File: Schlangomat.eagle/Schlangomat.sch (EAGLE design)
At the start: 38 parts, among them IC1 ULN2003AN, J1 Sensor1, J2 Sensor2, K1 36.11, K2 36.11, K3 36.11, K4 36.11, Q1 16MHz

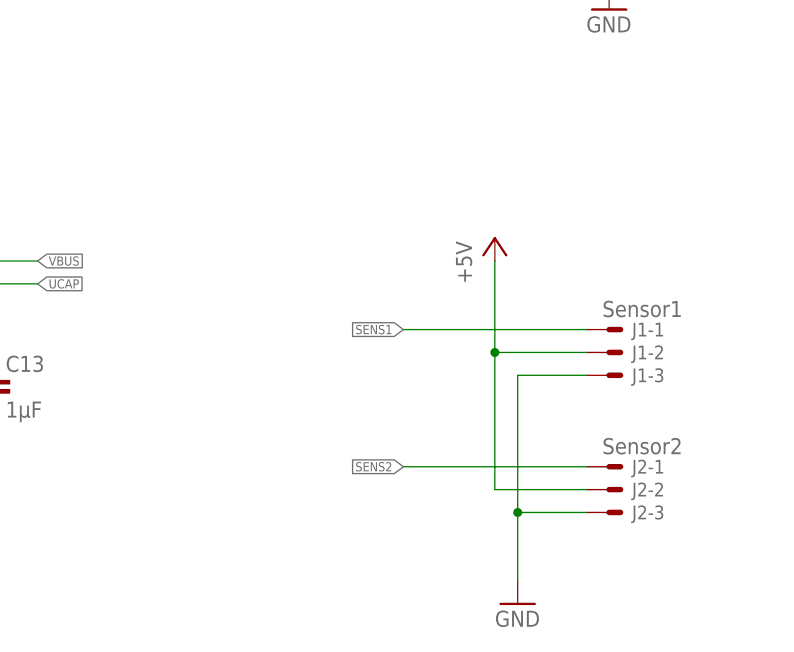
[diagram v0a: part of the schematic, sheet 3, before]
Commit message: Sensor-Support eingebaut
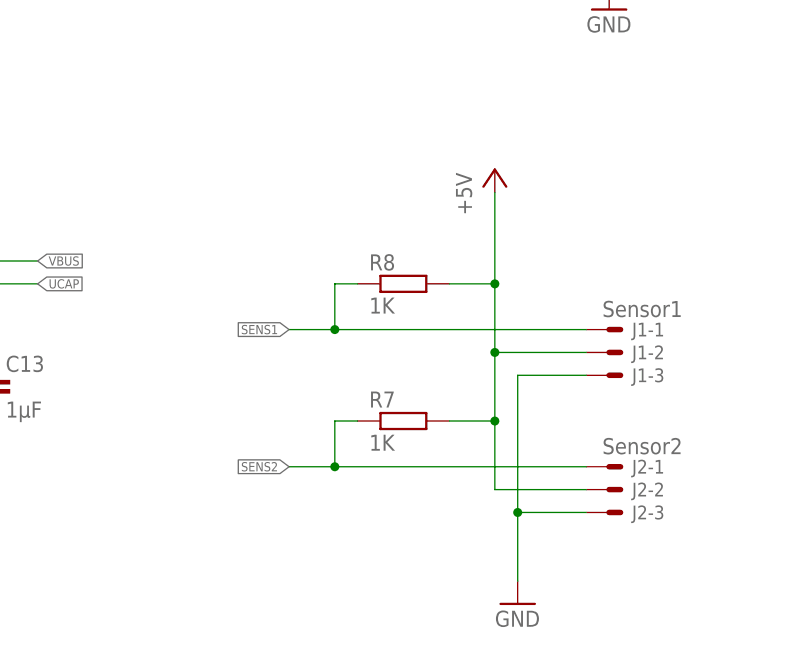
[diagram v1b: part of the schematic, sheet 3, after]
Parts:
- added R7, R8: 1K, rcl:R-EU_M0805
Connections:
- net +5V: now also R7.2, R8.2
- net SENS1: now also R8.1
- net SENS2: now also R7.1
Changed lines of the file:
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@@
 <part name="P+7" library="supply1" deviceset="+5V" device=""/>
 <part name="GND9" library="supply1" deviceset="GND" device=""/>
+<part name="R7" library="rcl" deviceset="R-EU_" device="M0805" value="1K"/>
+<part name="R8" library="rcl" deviceset="R-EU_" device="M0805" value="1K"/>
 </parts>
 <sheets>
@@
 <instance part="J2" gate="-2" x="185.42" y="0"/>
 <instance part="J2" gate="-3" x="185.42" y="-2.54"/>
-<instance part="P+7" gate="1" x="172.72" y="27.94"/>
+<instance part="P+7" gate="1" x="172.72" y="35.56"/>
 <instance part="GND9" gate="1" x="175.26" y="-12.7"/>
+<instance part="R7" gate="G$1" x="162.56" y="7.62"/>
+<instance part="R8" gate="G$1" x="162.56" y="22.86"/>
 </instances>
 <busses>
@@
 <pinref part="J2" gate="-2" pin="S"/>
 <wire x1="182.88" y1="0" x2="172.72" y2="0" width="0.1524" layer="91"/>
-<wire x1="172.72" y1="0" x2="172.72" y2="15.24" width="0.1524" layer="91"/>
+<wire x1="172.72" y1="0" x2="172.72" y2="7.62" width="0.1524" layer="91"/>
 <junction x="172.72" y="15.24"/>
 <pinref part="P+7" gate="1" pin="+5V"/>
-<wire x1="172.72" y1="25.4" x2="172.72" y2="15.24" width="0.1524" layer="91"/>
+<wire x1="172.72" y1="7.62" x2="172.72" y2="15.24" width="0.1524" layer="91"/>
+<wire x1="172.72" y1="33.02" x2="172.72" y2="22.86" width="0.1524" layer="91"/>
+<pinref part="R8" gate="G$1" pin="2"/>
+<wire x1="172.72" y1="22.86" x2="172.72" y2="15.24" width="0.1524" layer="91"/>
+<wire x1="172.72" y1="22.86" x2="167.64" y2="22.86" width="0.1524" layer="91"/>
+<junction x="172.72" y="22.86"/>
+<pinref part="R7" gate="G$1" pin="2"/>
+<wire x1="167.64" y1="7.62" x2="172.72" y2="7.62" width="0.1524" layer="91"/>
+<junction x="172.72" y="7.62"/>
 </segment>
 </net>
@@
 <segment>
 <pinref part="J1" gate="-1" pin="S"/>
-<wire x1="182.88" y1="17.78" x2="162.56" y2="17.78" width="0.1524" layer="91"/>
-<label x="162.56" y="17.78" size="1.016" layer="95" rot="R180" xref="yes"/>
+<wire x1="182.88" y1="17.78" x2="154.94" y2="17.78" width="0.1524" layer="91"/>
+<label x="149.86" y="17.78" size="1.016" layer="95" rot="R180" xref="yes"/>
+<pinref part="R8" gate="G$1" pin="1"/>
+<wire x1="154.94" y1="17.78" x2="149.86" y2="17.78" width="0.1524" layer="91"/>
+<wire x1="157.48" y1="22.86" x2="154.94" y2="22.86" width="0.1524" layer="91"/>
+<wire x1="154.94" y1="22.86" x2="154.94" y2="17.78" width="0.1524" layer="91"/>
+<junction x="154.94" y="17.78"/>
 </segment>
 </net>
@@
 <segment>
 <pinref part="J2" gate="-1" pin="S"/>
-<wire x1="182.88" y1="2.54" x2="162.56" y2="2.54" width="0.1524" layer="91"/>
-<label x="162.56" y="2.54" size="1.016" layer="95" rot="R180" xref="yes"/>
-</segment>
-</net>
+<wire x1="182.88" y1="2.54" x2="154.94" y2="2.54" width="0.1524" layer="91"/>
+<label x="149.86" y="2.54" size="1.016" layer="95" rot="R180" xref="yes"/>
+<pinref part="R7" gate="G$1" pin="1"/>
+<wire x1="154.94" y1="2.54" x2="149.86" y2="2.54" width="0.1524" layer="91"/>
+<wire x1="157.48" y1="7.62" x2="154.94" y2="7.62" width="0.1524" layer="91"/>
+<wire x1="154.94" y1="7.62" x2="154.94" y2="2.54" width="0.1524" layer="91"/>
+<junction x="154.94" y="2.54"/>
+</segment>
+</net>

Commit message: Board gelayoutet
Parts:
- removed IN: (no value), con-ptr500:AK500/2
- removed OUT: (no value), con-ptr500:AK500/4
- removed SENS1, SENS2: 22-27-2031-03, con-molex:22-27-2031-03
- added X1: AC-IN, con-wago:236-501-7,62
- added X2: AC-OUT-1, con-wago:236-501-7,62
- added X3: AC-OUT-2, con-wago:236-501-7,62
- added X4: AC-OUT-3, con-wago:236-501-7,62
- added X5: AC-OUT-4, con-wago:236-501-7,62
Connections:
- removed net AC_OUT_1: K1.P$4, OUT-1.KL
- removed net AC_OUT_2: K2.P$4, OUT-2.KL
- removed net AC_OUT_3: K3.P$4, OUT-3.KL
- removed net AC_OUT_4: K4.P$4, OUT-4.KL
- removed net PC6: EXT-6.S, U$1.PC6(OC3A/!OC4A)
- removed net PC7: EXT-7.S, U$1.PC7(ICP3/CLK0/OC4A)
- new net N$13: K3.P$4, X4.B1
- new net N$14: K4.P$4, X5.B1
- new net PF0: EXT-2.S, U$1.PF0(ADC0)
- new net PF1: EXT-3.S, U$1.PF1(ADC1)
- net +5V: no longer SENS1-3.S, SENS2-3.S
- net AC_IN: now also X1.B1; no longer IN-1.KL, IN-2.KL
- net GND: no longer SENS1-2.S, SENS2-2.S
- net N$10: now also K1.P$4, X2.B1; no longer SENS1-1.S, U$1.PF0(ADC0)
- net N$12: now also K2.P$4, X3.B1; no longer SENS2-1.S, U$1.PF1(ADC1)
- net PF4: now also EXT-4.S; no longer EXT-2.S
- net PF5: now also EXT-5.S; no longer EXT-3.S
- net PF6: now also EXT-6.S; no longer EXT-4.S
- net PF7: now also EXT-7.S; no longer EXT-5.S

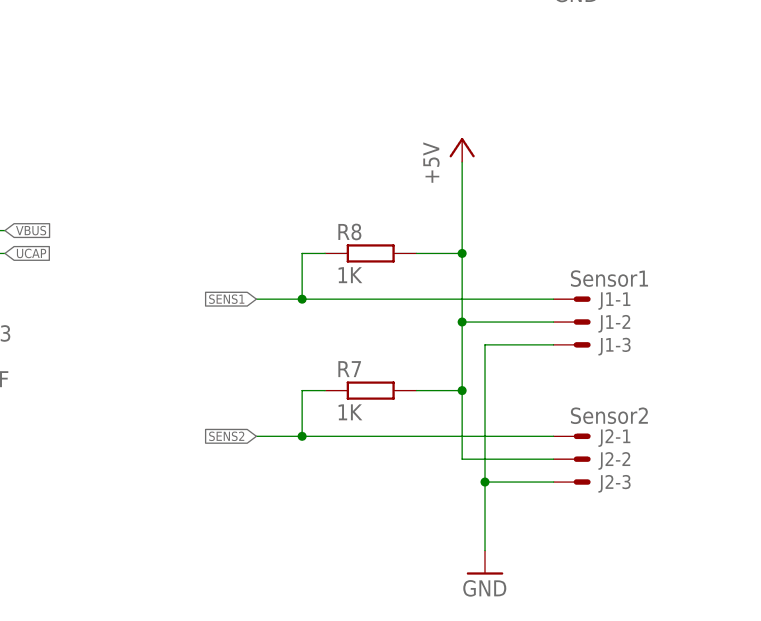
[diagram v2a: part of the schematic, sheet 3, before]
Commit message: PullUp-FuckUp gefixt, Fehlerbeseitigt
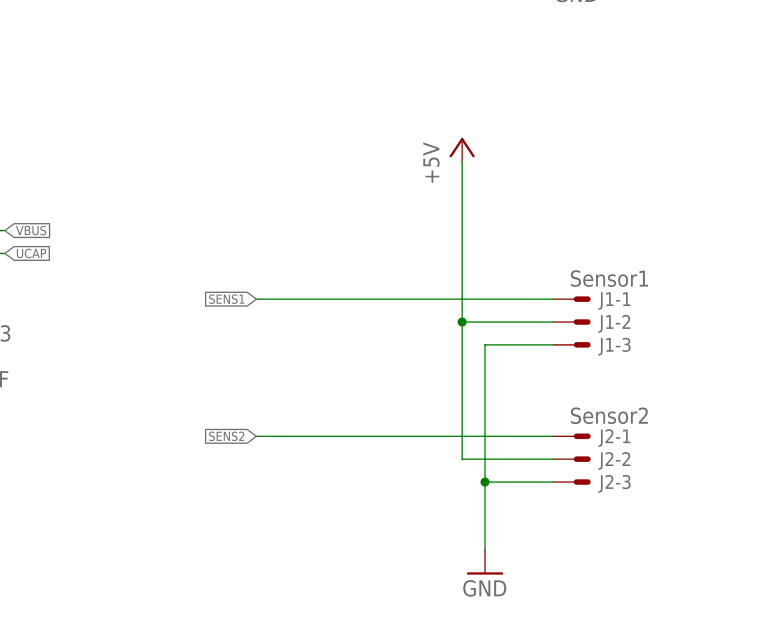
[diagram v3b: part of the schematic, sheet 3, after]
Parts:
- removed R7, R8: 1K, rcl:R-EU_M0805
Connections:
- net +5V: no longer R7.2, R8.2
- net SENS1: no longer R8.1
- net SENS2: no longer R7.1
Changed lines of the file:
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@@
 <part name="P+7" library="supply1" deviceset="+5V" device=""/>
 <part name="GND9" library="supply1" deviceset="GND" device=""/>
-<part name="R7" library="rcl" deviceset="R-EU_" device="M0805" value="1K"/>
-<part name="R8" library="rcl" deviceset="R-EU_" device="M0805" value="1K"/>
 <part name="X1" library="con-wago" deviceset="236" device="-7,62" technology="-501" value="AC-IN"/>
 <part name="X2" library="con-wago" deviceset="236" device="-7,62" technology="-501" value="AC-OUT-1"/>
@@
 <instance part="P+7" gate="1" x="172.72" y="35.56"/>
 <instance part="GND9" gate="1" x="175.26" y="-12.7"/>
-<instance part="R7" gate="G$1" x="162.56" y="7.62"/>
-<instance part="R8" gate="G$1" x="162.56" y="22.86"/>
 </instances>
 <busses>
@@
 <pinref part="J2" gate="-2" pin="S"/>
 <wire x1="182.88" y1="0" x2="172.72" y2="0" width="0.1524" layer="91"/>
-<wire x1="172.72" y1="0" x2="172.72" y2="7.62" width="0.1524" layer="91"/>
 <junction x="172.72" y="15.24"/>
 <pinref part="P+7" gate="1" pin="+5V"/>
-<wire x1="172.72" y1="7.62" x2="172.72" y2="15.24" width="0.1524" layer="91"/>
-<wire x1="172.72" y1="33.02" x2="172.72" y2="22.86" width="0.1524" layer="91"/>
-<pinref part="R8" gate="G$1" pin="2"/>
-<wire x1="172.72" y1="22.86" x2="172.72" y2="15.24" width="0.1524" layer="91"/>
-<wire x1="172.72" y1="22.86" x2="167.64" y2="22.86" width="0.1524" layer="91"/>
-<junction x="172.72" y="22.86"/>
-<pinref part="R7" gate="G$1" pin="2"/>
-<wire x1="167.64" y1="7.62" x2="172.72" y2="7.62" width="0.1524" layer="91"/>
-<junction x="172.72" y="7.62"/>
+<wire x1="172.72" y1="0" x2="172.72" y2="15.24" width="0.1524" layer="91"/>
+<wire x1="172.72" y1="33.02" x2="172.72" y2="15.24" width="0.1524" layer="91"/>
 </segment>
 </net>
@@
 <segment>
 <pinref part="J1" gate="-1" pin="S"/>
-<wire x1="182.88" y1="17.78" x2="154.94" y2="17.78" width="0.1524" layer="91"/>
+<wire x1="182.88" y1="17.78" x2="149.86" y2="17.78" width="0.1524" layer="91"/>
 <label x="149.86" y="17.78" size="1.016" layer="95" rot="R180" xref="yes"/>
-<pinref part="R8" gate="G$1" pin="1"/>
-<wire x1="154.94" y1="17.78" x2="149.86" y2="17.78" width="0.1524" layer="91"/>
-<wire x1="157.48" y1="22.86" x2="154.94" y2="22.86" width="0.1524" layer="91"/>
-<wire x1="154.94" y1="22.86" x2="154.94" y2="17.78" width="0.1524" layer="91"/>
-<junction x="154.94" y="17.78"/>
 </segment>
 </net>
@@
 <segment>
 <pinref part="J2" gate="-1" pin="S"/>
-<wire x1="182.88" y1="2.54" x2="154.94" y2="2.54" width="0.1524" layer="91"/>
+<wire x1="182.88" y1="2.54" x2="149.86" y2="2.54" width="0.1524" layer="91"/>
 <label x="149.86" y="2.54" size="1.016" layer="95" rot="R180" xref="yes"/>
-<pinref part="R7" gate="G$1" pin="1"/>
-<wire x1="154.94" y1="2.54" x2="149.86" y2="2.54" width="0.1524" layer="91"/>
-<wire x1="157.48" y1="7.62" x2="154.94" y2="7.62" width="0.1524" layer="91"/>
-<wire x1="154.94" y1="7.62" x2="154.94" y2="2.54" width="0.1524" layer="91"/>
-<junction x="154.94" y="2.54"/>
-</segment>
-</net>
+</segment>
+</net>
